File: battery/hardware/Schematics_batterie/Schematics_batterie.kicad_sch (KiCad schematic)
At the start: 24 parts, among them IC1 BQ25185DLHR, J1 USB_C_Receptacle_USB2.0_16P, J2 Conn_02x07_Odd_Even, J3 Conn_01x02, U1 BU33SD5WG-TR, U2 STM32G431KBTx, U3 USBLC6-2SC6

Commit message: réglage faits avec mr Fiack
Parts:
- C7: value 10 µF -> 4.7 µF
- R2, R4: value R_Small -> 5.1k
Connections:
- net DC Input is gone; now on net +5V: C1.1, IC1.10 (IN)
- net +5V: now also J1.A4 (VBUS), J1.A9 (VBUS), J1.B4 (VBUS), J1.B9 (VBUS)
- net GND: now also C11.2; no longer C11.1
- net NRST: now also C11.1; no longer C11.2
- net at J1.A6 (D+): now also J1.B6 (D+)
- net at J1.A7 (D-): now also J1.B7 (D-)
- no-connect marks 6 -> 9
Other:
- moved on the sheet: C10, C11, C6, C7, C8, C9, D1, L1, R1, U2

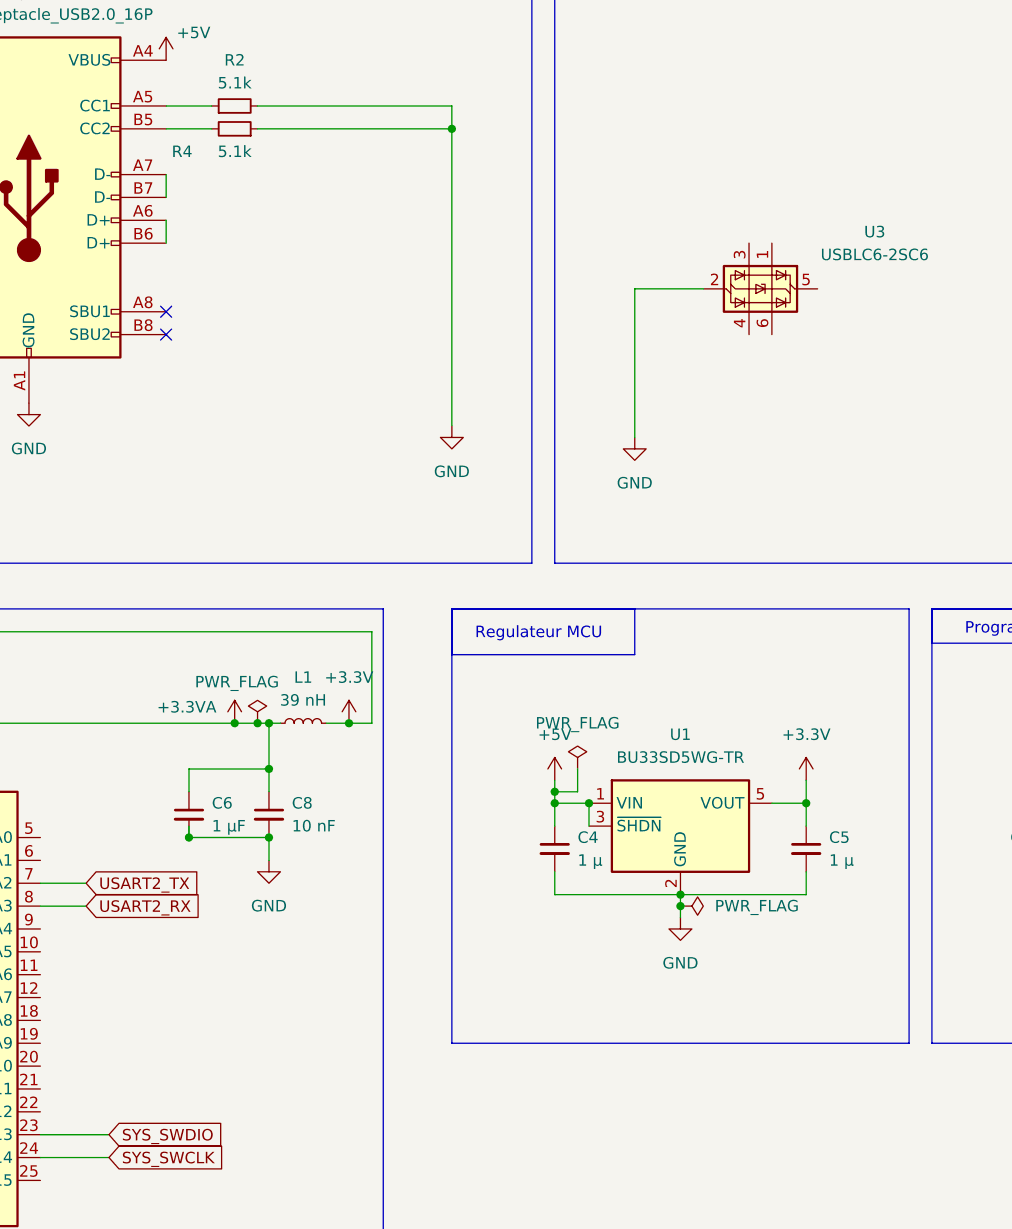
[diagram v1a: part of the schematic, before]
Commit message: ajout de l'ioc
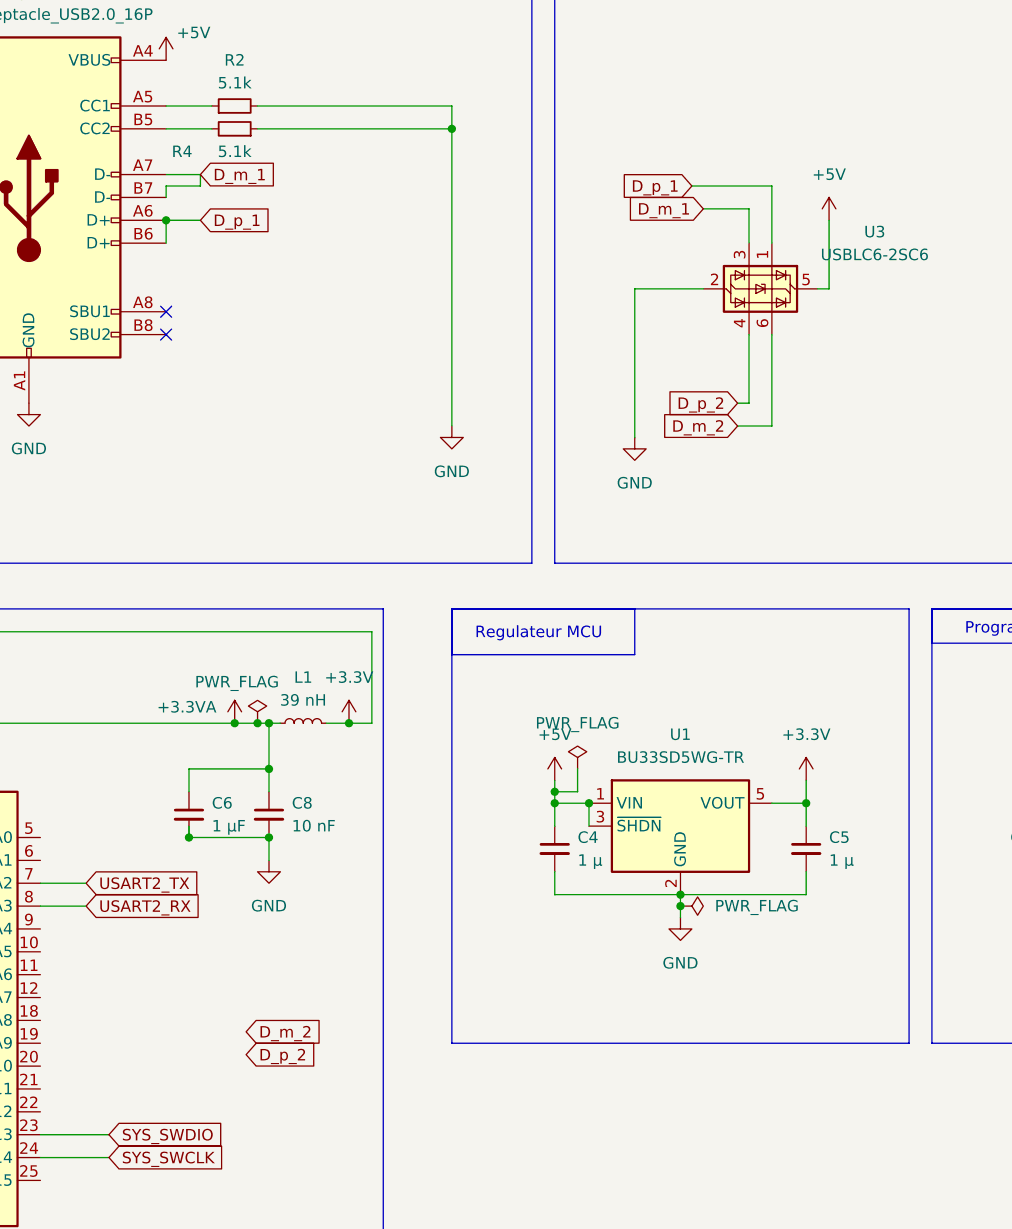
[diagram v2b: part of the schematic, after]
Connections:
- net +5V: now also U3.5 (VBUS)
- net D_p_1: now reaches U3.1 (I/O1)
- net D_p_1: now also J1.A6 (D+), J1.B6 (D+)
- net D_m_1: now reaches U3.3 (I/O2)
- net D_m_1: now also J1.A7 (D-), J1.B7 (D-)
- net D_p_2: now reaches U3.4 (I/O2)
- net D_m_2: now reaches U3.6 (I/O1)

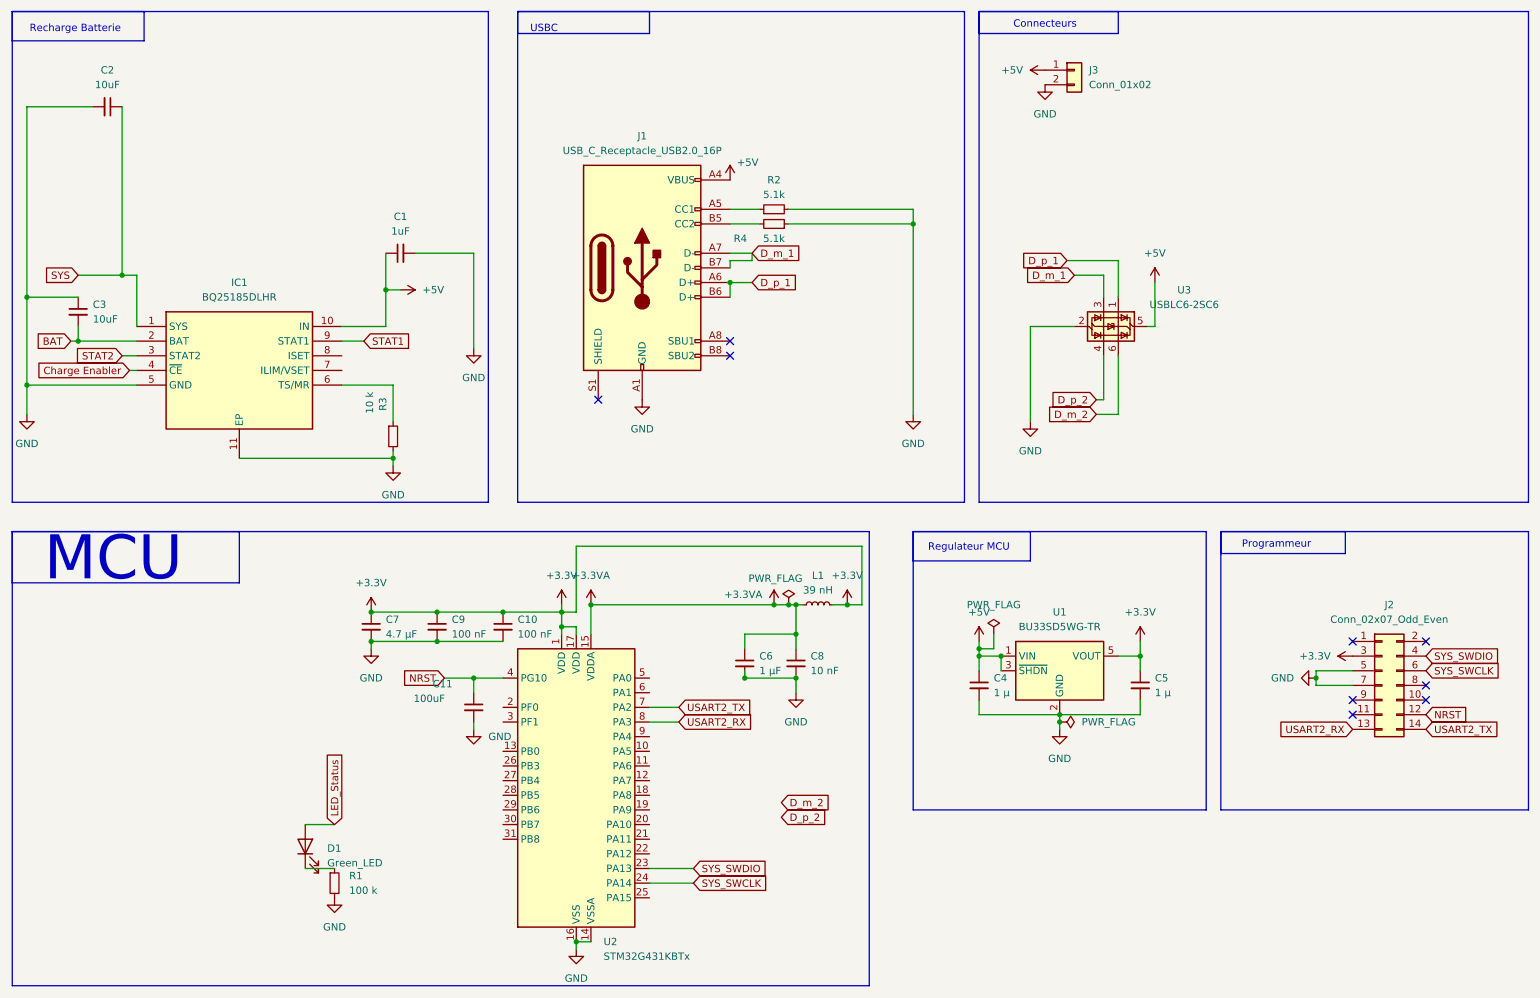
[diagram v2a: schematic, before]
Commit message: mise a jour du schematics, nouveau programmeur, connection de D+ et D-
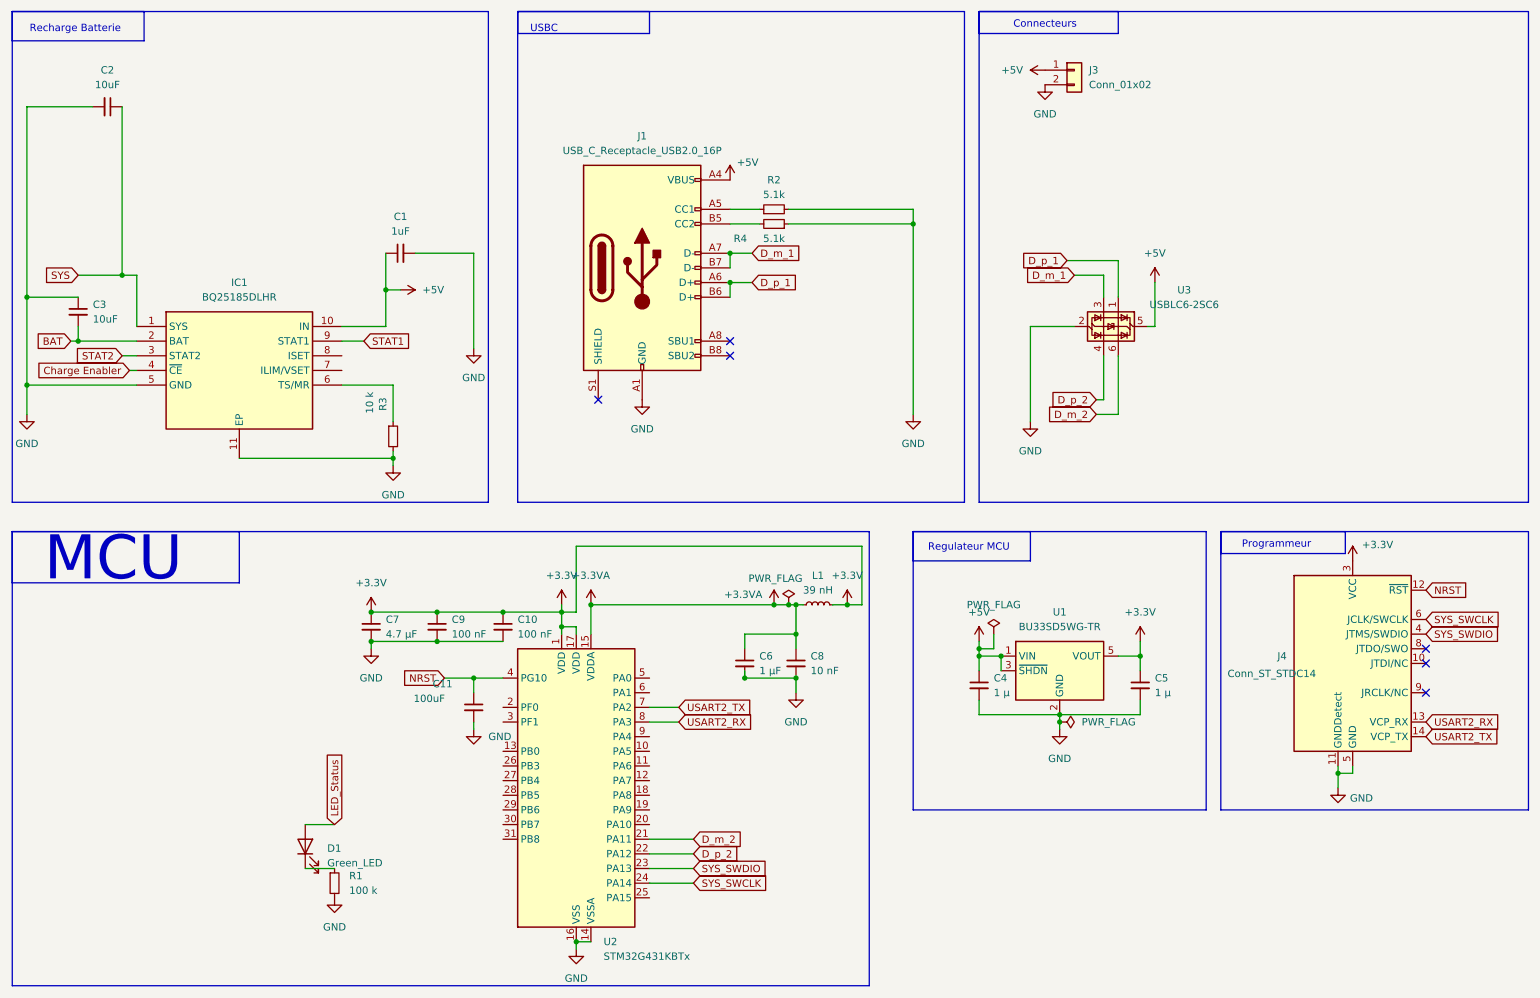
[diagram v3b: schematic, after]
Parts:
- removed J2: Conn_02x07_Odd_Even, Connector_PinHeader_1.27mm:PinHeader_2x07_P1.27mm_Vertical_SMD, symbol Connector_Generic:Conn_02x07_Odd_Even
- added J4: Conn_ST_STDC14, symbol Connector:Conn_ST_STDC14
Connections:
- net +3.3V: now also J4.3 (VCC)
- net D_m_2: now also U2.21 (PA11)
- net D_p_2: now also U2.22 (PA12)
- net GND: now also J4.11 (GNDDetect), J4.5 (GND), J4.7 (GND)
- net NRST: now also J4.12 (~{RST})
- net SYS_SWCLK: now also J4.6 (JCLK/SWCLK)
- net SYS_SWDIO: now also J4.4 (JTMS/SWDIO)
- net USART2_RX: now also J4.13 (VCP_RX)
- net USART2_TX: now also J4.14 (VCP_TX)
- no-connect marks 9 -> 6

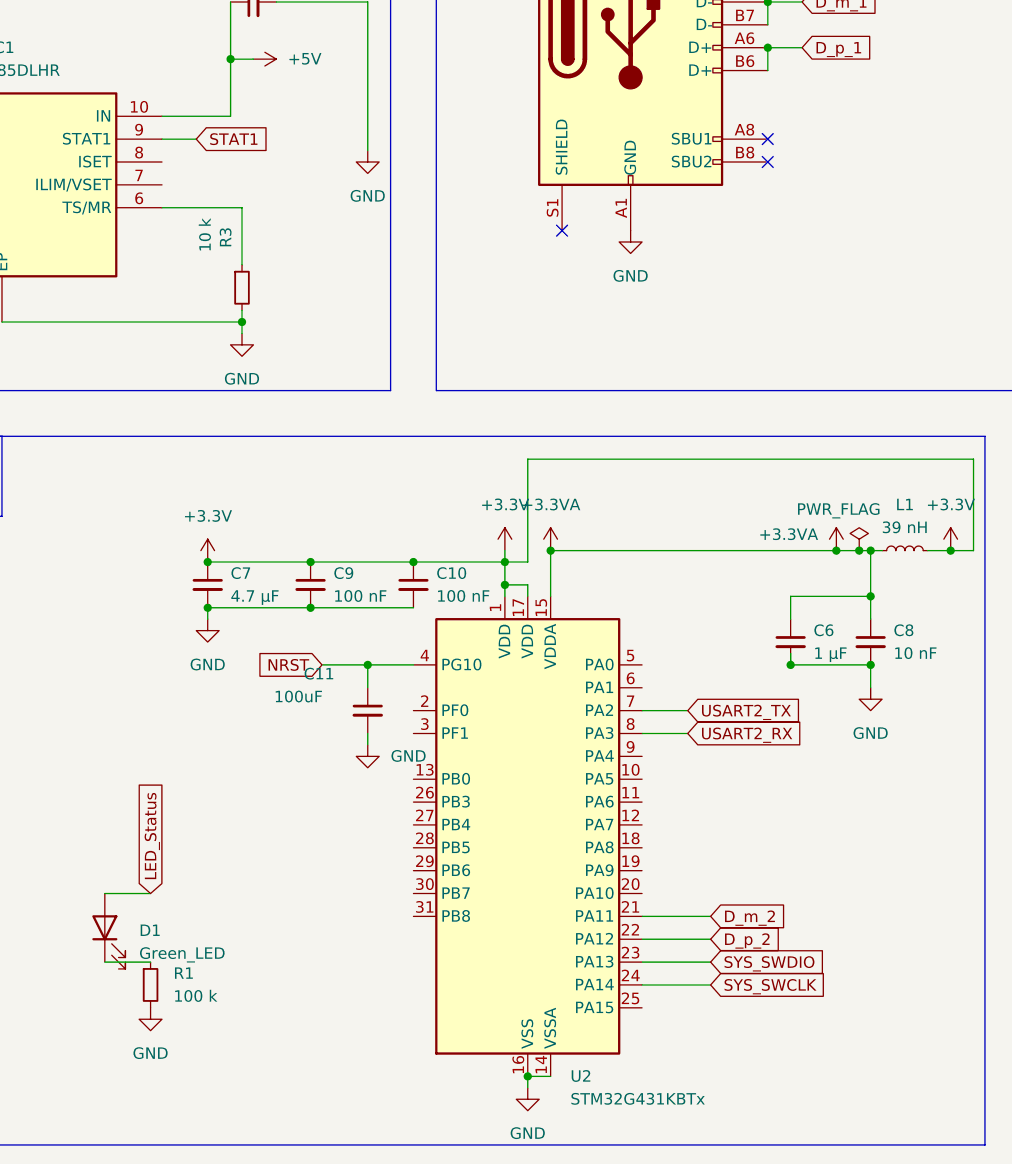
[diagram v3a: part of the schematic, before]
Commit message: dernière configuration, rajouter encore certaines empreintes, ILIM et ISET réglé
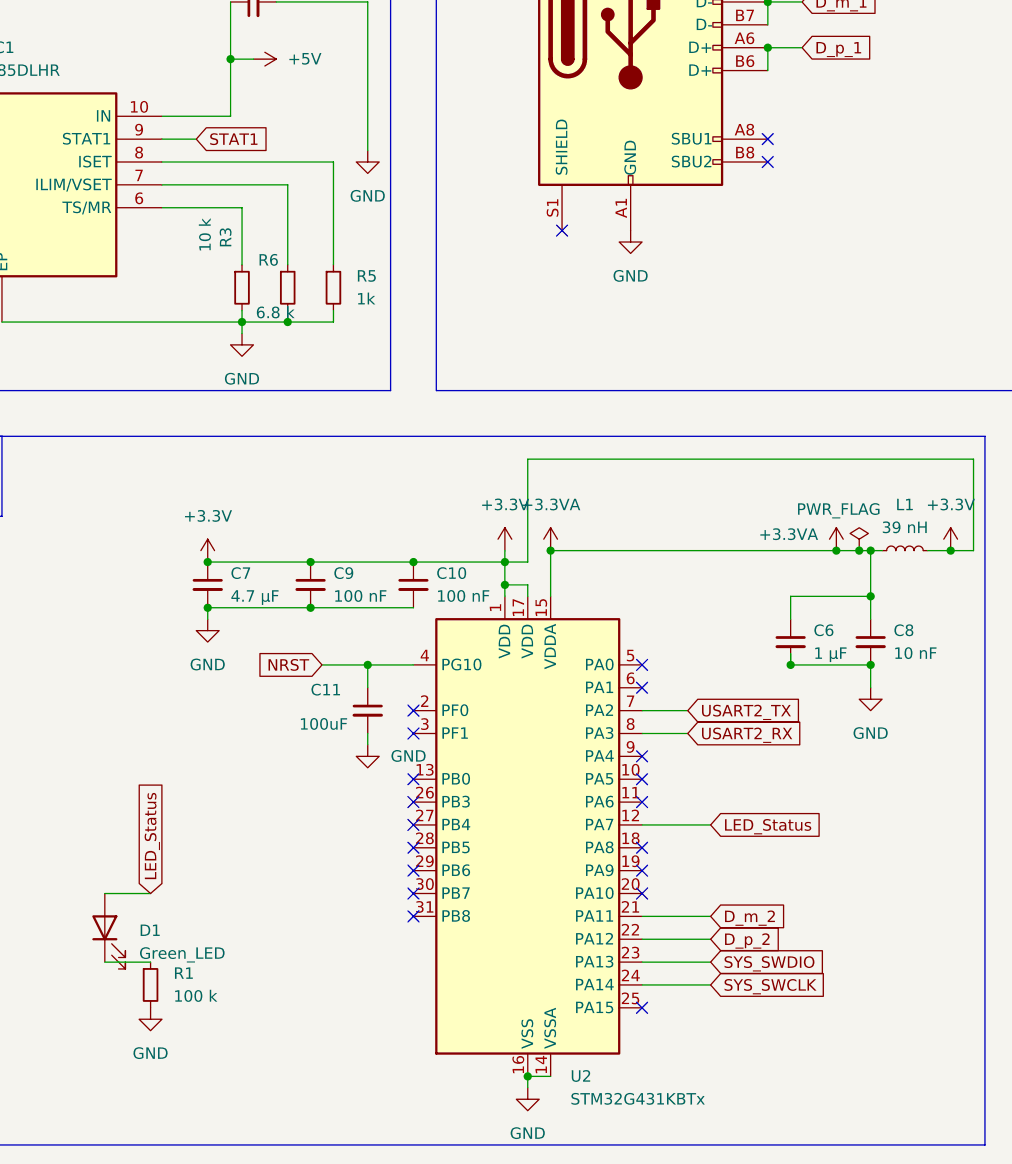
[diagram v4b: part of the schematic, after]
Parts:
- added R5: 1k, symbol Device:R_Small
- added R6: 6.8 k, symbol Device:R_Small
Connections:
- net GND: now also R5.2, R6.2
- net LED_Status: now also U2.12 (PA7)
- net at IC1.7 (ILIM/VSET): now also R6.1
- net at IC1.8 (ISET): now also R5.1
- no-connect marks 6 -> 24
